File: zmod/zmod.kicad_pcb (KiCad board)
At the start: 6 copper layers, 50 x 70 mm, 13 parts, among them J2 QTH-020-01-X-D-DP-A

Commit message: routed zmod
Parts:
- moved D2 25.3 mm to (121.6, 91.3)
- moved D1 25.3 mm to (124.6, 91.3)
- moved R1 25.1 mm to (124.6, 86.7)
- moved R2 25.1 mm to (121.6, 86.7)
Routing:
- net /hss0_N: track 0.00 -> 352.3 mm, vias 0 -> 12
- net /hss0_P: track 0.00 -> 352.0 mm, vias 0 -> 12
- net Net-(J2-Pad14): track 0.00 -> 54.8 mm, vias 0 -> 2
- net Net-(J2-Pad16): track 0.00 -> 54.7 mm, vias 0 -> 2
- net /lvdsclk_P: track 0.00 -> 27.8 mm
- net /lvdsclk_N: track 0.00 -> 27.7 mm
- net /lvds1_P: track 0.00 -> 10.7 mm, vias 0 -> 2
- net /lvds1_N: track 0.00 -> 10.6 mm, vias 0 -> 2
- net /lvds0_N: track 0.00 -> 10.5 mm, vias 0 -> 2
- net /lvds0_P: track 0.00 -> 10.4 mm, vias 0 -> 2
- net /hss1_P: track 0.00 -> 9.98 mm
- net /hss1_N: track 0.00 -> 9.91 mm
- net /lvds3_N: track 0.00 -> 8.32 mm, vias 0 -> 2
- net GND: track 0.00 -> 8.19 mm, vias 0 -> 8
- net /lvds2_N: track 0.00 -> 7.95 mm, vias 0 -> 2
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- removed copper zone on In2.Cu, net GND
- removed copper zone on In3.Cu, net GND

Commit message: ready for fab, I think.
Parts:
- moved R3 0.54 mm to (127.5, 68.1)
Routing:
- net /hss0_N: track 352.3 -> 6.39 mm, vias 12 -> 0
- net /hss0_P: track 352.0 -> 6.39 mm, vias 12 -> 0
- net /hss1_N: track 9.91 -> 352.4 mm, vias 0 -> 12
- net /hss1_P: track 9.98 -> 348.1 mm, vias 0 -> 12
- net /lvdsclk_N: track 27.7 -> 24.2 mm
- net /lvds2_P: track 6.10 -> 8.56 mm
- net Net-(J2-Pad14): track 54.8 -> 52.9 mm
- net Net-(J2-Pad16): track 54.7 -> 52.8 mm
- net /lvds1_P: track 10.7 -> 12.5 mm
- net /lvds3_N: track 8.32 -> 6.54 mm
- net /lvds0_P: track 10.4 -> 12.1 mm
- net /lvds1_N: track 10.6 -> 12.1 mm
- net GND: track 8.19 -> 9.25 mm, vias 8 -> 10
- net +3V3: track 1.17 -> 2.19 mm, vias 1 -> 2
- net /lvds3_P: track 6.63 -> 7.34 mm
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
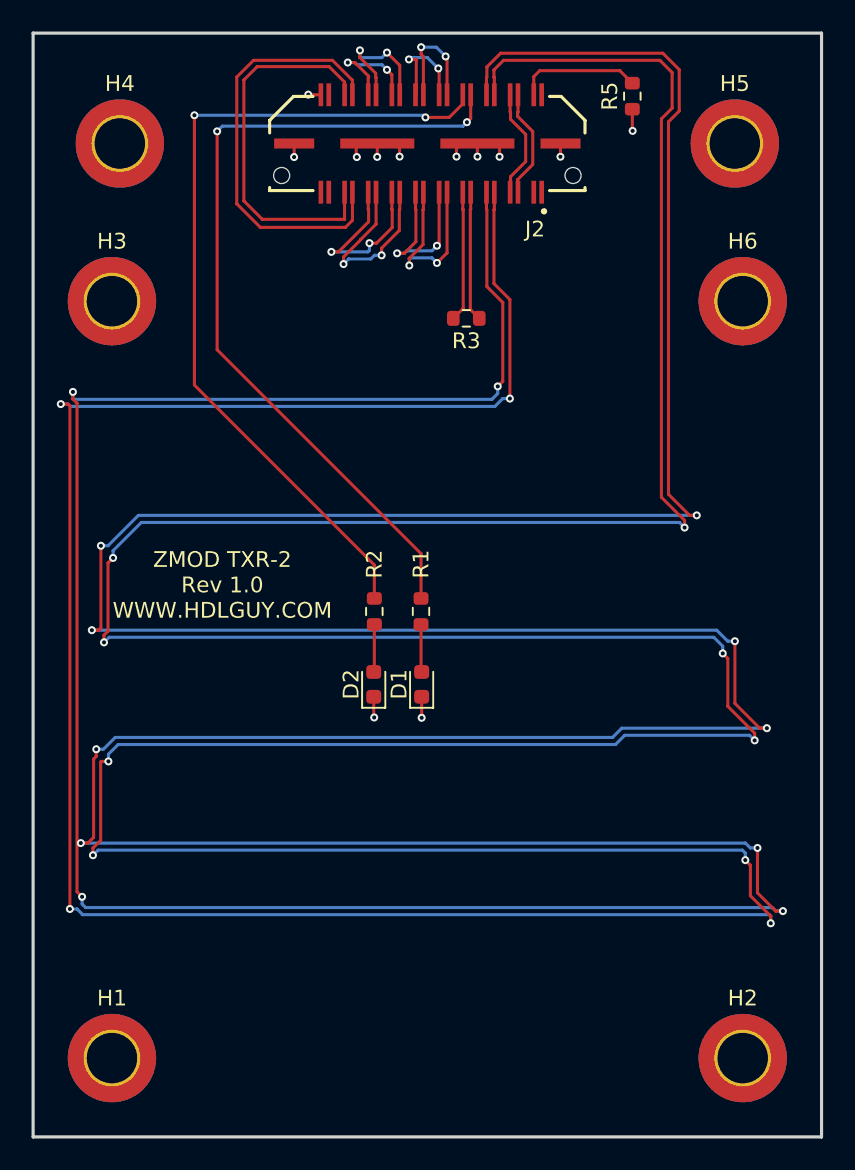
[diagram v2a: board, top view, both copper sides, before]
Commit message: cleaned up hss diff-pair
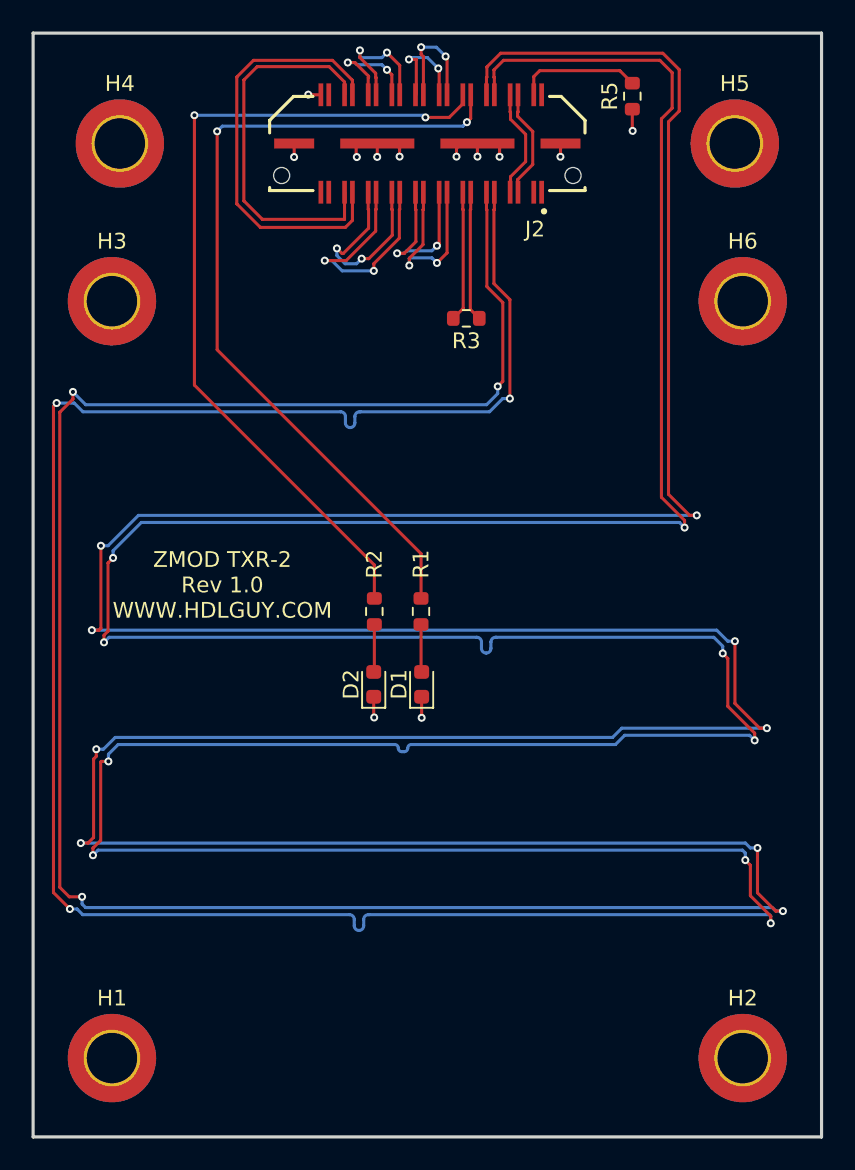
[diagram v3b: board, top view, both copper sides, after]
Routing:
- net /hss1_P: track 348.1 -> 353.5 mm
- net /lvds1_P: track 12.5 -> 15.5 mm
- net /hss1_N: track 352.4 -> 353.6 mm
- net /lvds1_N: track 12.1 -> 12.8 mm
